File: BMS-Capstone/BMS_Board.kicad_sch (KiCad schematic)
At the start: 0 parts

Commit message: Added MP chip
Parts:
- added IC1: MP2639AGR-Z, MP2639AGRZ, symbol SamacSys_Parts:MP2639AGR-Z
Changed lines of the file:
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@@
 	(generator_version "9.0")
 	(paper "A4")
+	(symbol
+		(lib_id "SamacSys_Parts:MP2639AGR-Z")
+		(at 115.57 81.28 0)
+		(unit 1)
+		(exclude_from_sim no)
+		(in_bom yes)
+		(on_board yes)
+		(dnp no)
+		(fields_autoplaced yes)
+		(property "Reference" "IC1"
+			(at 111.76 74.8598 0)
+			(effects
+				(font
+					(size 1.27 1.27)
+				)
+			)
+		)
+		(property "Value" "MP2639AGR-Z"
+			(at 111.76 77.3998 0)
+			(effects
+				(font
+					(size 1.27 1.27)
+				)
+			)
+		)
+		(property "Footprint" "MP2639AGRZ"
+			(at 142.24 166.04 0)
+			(effects
+				(font
+					(size 1.27 1.27)
+				)
+				(justify left top)
+				(hide yes)
+			)
+		)
+		(property "Datasheet" "http://www.monolithicpower.com/pub/media/document/MP2639A_r1.0.pdf"
+			(at 142.24 266.04 0)
+			(effects
+				(font
+					(size 1.27 1.27)
+				)
+				(justify left top)
+				(hide yes)
+			)
+		)
+		(property "Description" "Battery Management 2-Cell 2.5A Li-ion or Li-polymer Switching Charger Integrated Bidirectional Charge/Discharge"
+			(at 115.57 81.28 0)
+			(effects
+				(font
+					(size 1.27 1.27)
+				)
+				(hide yes)
+			)
+		)
+		(property "Height" "1"
+			(at 142.24 466.04 0)
+			(effects
+				(font
+					(size 1.27 1.27)
+				)
+				(justify left top)
+				(hide yes)
+			)
+		)
+		(property "Manufacturer_Name" "Monolithic Power Systems (MPS)"
+			(at 142.24 566.04 0)
+			(effects
+				(font
+					(size 1.27 1.27)
+				)
+				(justify left top)
+				(hide yes)
+			)
+		)
+		(property "Manufacturer_Part_Number" "MP2639AGR-Z"
+			(at 142.24 666.04 0)
+			(effects
+				(font
+					(size 1.27 1.27)
+				)
+				(justify left top)
+				(hide yes)
+			)
+		)
+		(property "Mouser Part Number" "946-MP2639AGR-Z"
+			(at 142.24 766.04 0)
+			(effects
+				(font
+					(size 1.27 1.27)
+				)
+				(justify left top)
+				(hide yes)
+			)
+		)
+		(property "Mouser Price/Stock" "https://www.mouser.co.uk/ProductDetail/Monolithic-Power-Systems-MPS/MP2639AGR-Z?qs=YCa%2FAAYMW004W5DDRZSXeQ%3D%3D"
+			(at 142.24 866.04 0)
+			(effects
+				(font
+					(size 1.27 1.27)
+				)
+				(justify left top)
+				(hide yes)
+			)
+		)
+		(property "Arrow Part Number" ""
+			(at 142.24 966.04 0)
+			(effects
+				(font
+					(size 1.27 1.27)
+				)
+				(justify left top)
+				(hide yes)
+			)
+		)
+		(property "Arrow Price/Stock" ""
+			(at 142.24 1066.04 0)
+			(effects
+				(font
+					(size 1.27 1.27)
+				)
+				(justify left top)
+				(hide yes)
+			)
+		)
+		(pin "6"
+		)
+		(pin "25"
+		)
+		(pin "9"
+		)
+		(pin "22"
+		)
+		(pin "5"
+		)
+		(pin "7"
+		)
+		(pin "21"
+		)
+		(pin "23"
+		)
+		(pin "24"
+		)
+		(pin "8"
+		)
+		(pin "14"
+		)
+		(pin "2"
+		)
+		(pin "3"
+		)
+		(pin "1"
+		)
+		(pin "4"
+		)
+		(pin "26"
+		)
+		(pin "10"
+		)
+		(pin "12"
+		)
+		(pin "19"
+		)
+		(pin "20"
+		)
+		(pin "15"
+		)
+		(pin "11"
+		)
+		(pin "18"
+		)
+		(pin "17"
+		)
+		(pin "16"
+		)
+		(pin "13"
+		)
+		(instances
+			(project ""
+				(path "/f2da9442-ca05-4687-a880-d5cd24c39f1d/3dc06e74-ff57-4ce5-be5c-5d780b9552b6"
+					(reference "IC1")
+					(unit 1)
+				)
+			)
+		)
+	)
 )

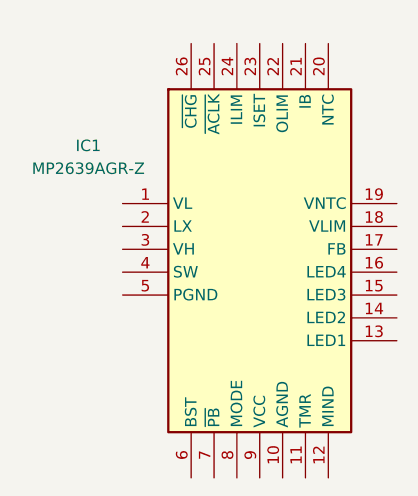
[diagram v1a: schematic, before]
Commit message: Added symbol and footprint for MP
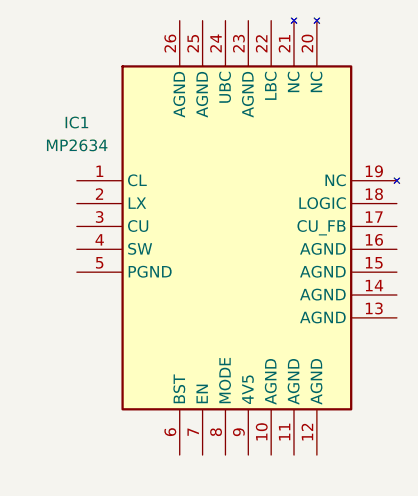
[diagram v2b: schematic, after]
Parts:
- removed IC1: MP2639AGR-Z, MP2639AGRZ, symbol SamacSys_Parts:MP2639AGR-Z
- added IC1: MP2634, SamacSys_Parts:MP2634, symbol SamacSys_Parts:MP2634
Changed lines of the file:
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@@
 	(paper "A4")
 	(symbol
-		(lib_id "SamacSys_Parts:MP2639AGR-Z")
-		(at 115.57 81.28 0)
+		(lib_id "SamacSys_Parts:MP2634")
+		(at 115.57 78.74 0)
 		(unit 1)
 		(exclude_from_sim no)
@@
 		(fields_autoplaced yes)
 		(property "Reference" "IC1"
-			(at 111.76 74.8598 0)
+			(at 110.49 72.3198 0)
 			(effects
 				(font
@@
 			)
 		)
-		(property "Value" "MP2639AGR-Z"
-			(at 111.76 77.3998 0)
+		(property "Value" "MP2634"
+			(at 110.49 74.8598 0)
 			(effects
 				(font
@@
 			)
 		)
-		(property "Footprint" "MP2639AGRZ"
-			(at 142.24 166.04 0)
+		(property "Footprint" "SamacSys_Parts:MP2634"
+			(at 142.24 163.5 0)
 			(effects
 				(font
@@
 		)
 		(property "Datasheet" "http://www.monolithicpower.com/pub/media/document/MP2639A_r1.0.pdf"
-			(at 142.24 266.04 0)
+			(at 142.24 263.5 0)
 			(effects
 				(font
@@
 			)
 		)
-		(property "Description" "Battery Management 2-Cell 2.5A Li-ion or Li-polymer Switching Charger Integrated Bidirectional Charge/Discharge"
-			(at 115.57 81.28 0)
+		(property "Description" "Integrated, 2A, BidirectionalActive Balancer"
+			(at 128.016 49.53 0)
 			(effects
 				(font
@@
 		)
 		(property "Height" "1"
-			(at 142.24 466.04 0)
+			(at 142.24 463.5 0)
 			(effects
 				(font
@@
 		)
 		(property "Manufacturer_Name" "Monolithic Power Systems (MPS)"
-			(at 142.24 566.04 0)
+			(at 142.24 563.5 0)
 			(effects
 				(font
@@
 		)
 		(property "Manufacturer_Part_Number" "MP2639AGR-Z"
-			(at 142.24 666.04 0)
+			(at 142.24 663.5 0)
 			(effects
 				(font
@@
 		)
 		(property "Mouser Part Number" "946-MP2639AGR-Z"
-			(at 142.24 766.04 0)
+			(at 142.24 763.5 0)
 			(effects
 				(font
@@
 		)
 		(property "Mouser Price/Stock" "https://www.mouser.co.uk/ProductDetail/Monolithic-Power-Systems-MPS/MP2639AGR-Z?qs=YCa%2FAAYMW004W5DDRZSXeQ%3D%3D"
-			(at 142.24 866.04 0)
+			(at 142.24 863.5 0)
 			(effects
 				(font
@@
 		)
 		(property "Arrow Part Number" ""
-			(at 142.24 966.04 0)
+			(at 142.24 963.5 0)
 			(effects
 				(font
@@
 		)
 		(property "Arrow Price/Stock" ""
-			(at 142.24 1066.04 0)
+			(at 142.24 1063.5 0)
 			(effects
 				(font
@@
 		(pin "6"
 		)
-		(pin "25"
+		(pin "18"
 		)
-		(pin "9"
+		(pin "20"
+		)
+		(pin "15"
+		)
+		(pin "1"
 		)
 		(pin "22"
 		)
-		(pin "5"
+		(pin "25"
 		)
-		(pin "7"
-		)
-		(pin "21"
-		)
-		(pin "23"
-		)
-		(pin "24"
-		)
-		(pin "8"
-		)
-		(pin "14"
-		)
-		(pin "2"
-		)
-		(pin "3"
-		)
-		(pin "1"
-		)
-		(pin "4"
+		(pin "11"
 		)
 		(pin "26"
@@
 		(pin "10"
 		)
-		(pin "12"
+		(pin "21"
+		)
+		(pin "7"
+		)
+		(pin "5"
+		)
+		(pin "24"
 		)
 		(pin "19"
 		)
-		(pin "20"
+		(pin "23"
 		)
-		(pin "15"
+		(pin "9"
 		)
-		(pin "11"
+		(pin "2"
 		)
-		(pin "18"
+		(pin "8"
+		)
+		(pin "3"
+		)
+		(pin "4"
+		)
+		(pin "12"
 		)
 		(pin "17"
@@
 		(pin "13"
 		)
+		(pin "14"
+		)
 		(instances

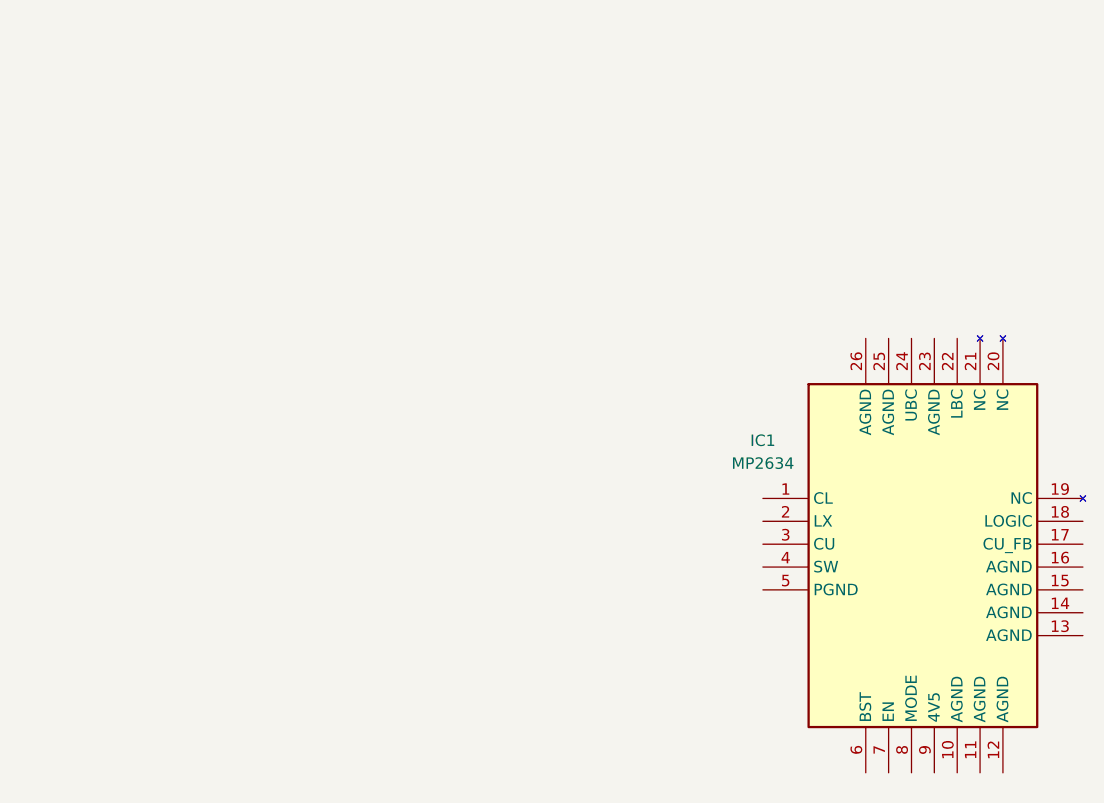
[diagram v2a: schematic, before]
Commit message: Created Schematic for MP chip
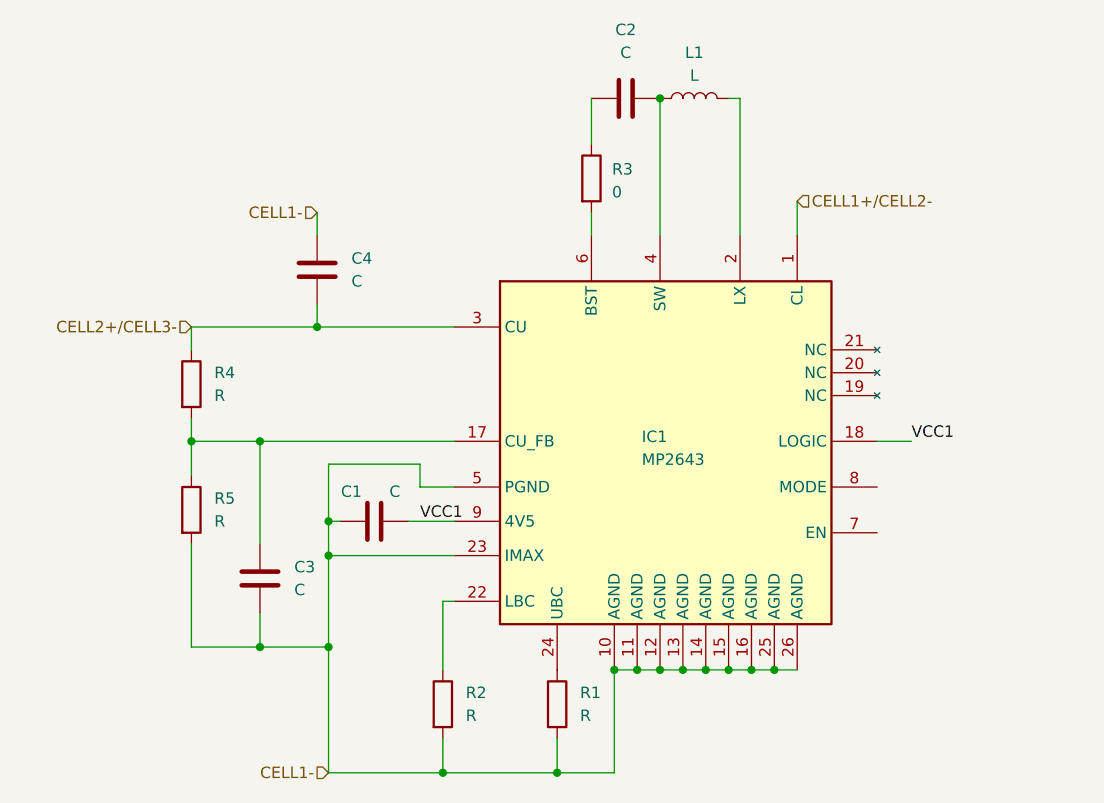
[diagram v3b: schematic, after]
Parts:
- removed IC1: MP2634, SamacSys_Parts:MP2634, symbol SamacSys_Parts:MP2634
- added C1, C2, C3, C4: C, Capacitor_SMD:C_0805_2012Metric, symbol Device:C
- added IC1: MP2643, SamacSys_Parts:MP2639AGRZ, symbol SamacSys_Parts:MP2643
- added L1: L, symbol Device:L
- added R1, R2, R4, R5: R, Resistor_SMD:R_0805_2012Metric, symbol Device:R
- added R3: 0, Resistor_SMD:R_0805_2012Metric, symbol Device:R
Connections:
- new net: C3.2, IC1.17 (CU_FB), R4.2, R5.1
- new net: C2.2, IC1.4 (SW), L1.1
- new net: IC1.2 (LX), L1.2
- new net: IC1.22 (LBC), R2.1
- new net: IC1.24 (UBC), R1.1
- new net: IC1.6 (BST), R3.2
- new net: C2.1, R3.1
- new net CELL1+/CELL2-: IC1.1 (CL)
- new net CELL1-: C1.1, C3.1, C4.2, IC1.10 (AGND), IC1.11 (AGND), IC1.12 (AGND), IC1.13 (AGND), IC1.14 (AGND), IC1.15 (AGND), IC1.16 (AGND), IC1.23 (IMAX), IC1.25 (AGND), IC1.26 (AGND), IC1.5 (PGND), R1.2, R2.2, R5.2
- new net CELL2+/CELL3-: C4.1, IC1.3 (CU), R4.1
- new net VCC1: C1.2, IC1.18 (LOGIC), IC1.9 (4V5)

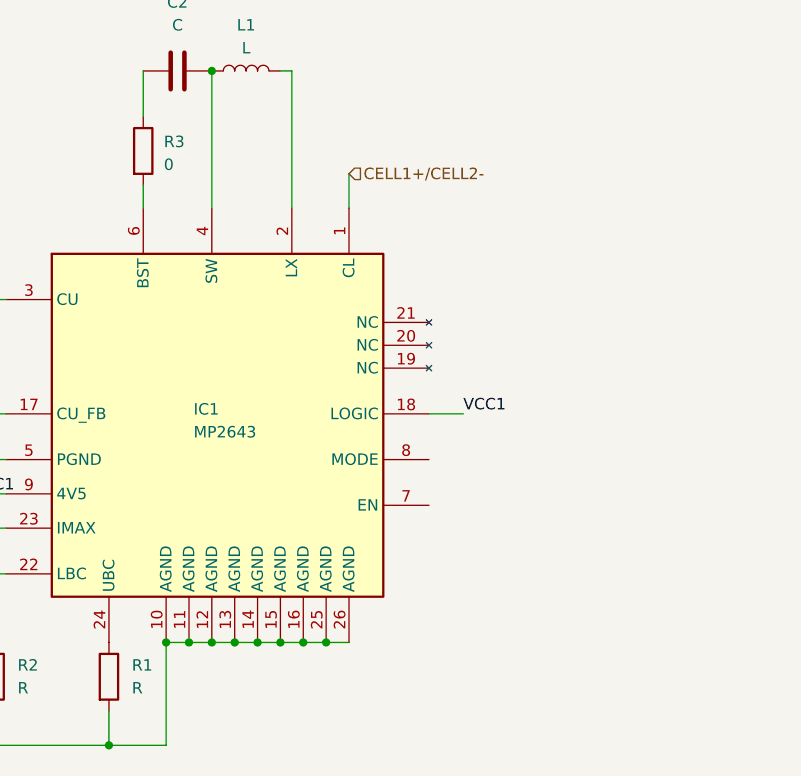
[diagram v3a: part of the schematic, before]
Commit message: Designed one entire MP chip layout
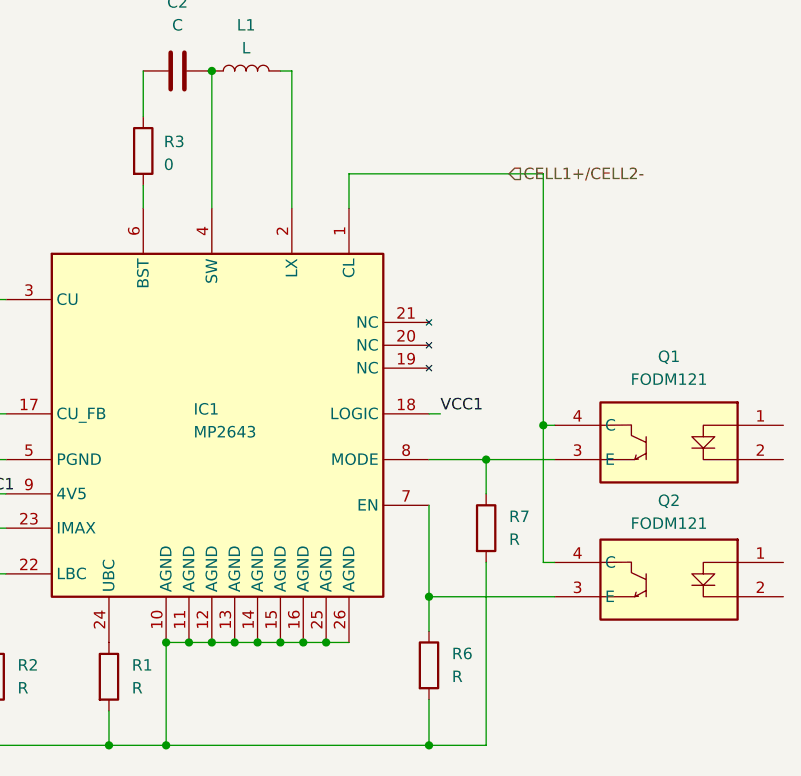
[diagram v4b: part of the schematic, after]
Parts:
- added Q1, Q2: FODM121, SOP254P675X240-4N, symbol SamacSys_Parts:FODM121
- added R6, R7: R, Resistor_SMD:R_0805_2012Metric, symbol Device:R
- L1: footprint (none) -> SamacSys_Parts:MPLAL4020R47 Inductor
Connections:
- net CELL1+/CELL2-: now also Q1.4 (C), Q2.4 (C)
- net CELL1-: now also R6.2, R7.2
- net at IC1.7 (EN): now also Q2.3 (E), R6.1
- net at IC1.8 (MODE): now also Q1.3 (E), R7.1

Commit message: More fixes
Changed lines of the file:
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@@
-	(wire
-		(pts
-			(xy 135.89 45.72) (xy 114.3 45.72)
-		)
-		(stroke
-			(width 0)
-			(type default)
-		)
-	)
 	(wire
 		(pts
@@
 		(pts
 			(xy 46.99 72.39) (xy 54.61 72.39)
+		)
+		(stroke
+			(width 0)
+			(type default)
+		)
+	)
+	(wire
+		(pts
+			(xy 114.3 45.72) (xy 135.89 45.72)
 		)
 		(stroke
@@
 	(hierarchical_label "CELL1+{slash}CELL2-"
 		(shape input)
-		(at 132.08 45.72 0)
-		(effects
-			(font
+		(at 135.89 45.72 0)
+		(effects
+			(font

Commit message: added CL capacitor
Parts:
- added C5: C, Capacitor_SMD:C_0805_2012Metric, symbol Device:C
- Q1, Q2: footprint SOP254P675X240-4N -> SamacSys_Parts:SOP254P675X240-4N
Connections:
- net CELL1+/CELL2-: now also C5.1
- net CELL1-: now also C5.2
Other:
- moved on the sheet: C1, C2, C3, C4, IC1, L1, Q1, Q2, R1, R2, R3, R4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

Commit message: Slight modifications
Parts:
- added C10, C6, C7, C8, C9: C, Capacitor_SMD:C_0805_2012Metric, symbol Device:C
- added IC2: MP2643, SamacSys_Parts:MP2639AGRZ, symbol SamacSys_Parts:MP2643
- added L2: L, SamacSys_Parts:MPLAL4020R47 Inductor, symbol Device:L
- added Q3, Q4: FODM121, SamacSys_Parts:SOP254P675X240-4N, symbol SamacSys_Parts:FODM121
- added R10: 0, Resistor_SMD:R_0805_2012Metric, symbol Device:R
- added R11, R12, R13, R14, R8, R9: R, Resistor_SMD:R_0805_2012Metric, symbol Device:R
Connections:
- net CELL1+/CELL2-: now also C10.2, C6.1, C7.2, C8.1, IC2.10 (AGND), IC2.11 (AGND), IC2.12 (AGND), IC2.13 (AGND), IC2.14 (AGND), IC2.15 (AGND), IC2.16 (AGND), IC2.23 (IMAX), IC2.25 (AGND), IC2.26 (AGND), IC2.5 (PGND), R10.2, R11.2, R13.2, R14.2, R9.2
- net CELL2+/CELL3-: now also C10.1, IC2.1 (CL), Q3.4 (C), Q4.4 (C)
- new net: IC2.7 (EN), Q4.3 (E), R13.1
- new net: IC2.8 (MODE), Q3.3 (E), R14.1
- new net: C9.1, R12.1
- new net: C9.2, IC2.4 (SW), L2.1
- new net: C6.2, IC2.17 (CU_FB), R8.2, R9.1
- new net: IC2.22 (LBC), R10.1
- new net: IC2.2 (LX), L2.2
- new net: IC2.24 (UBC), R11.1
- new net: IC2.6 (BST), R12.2
- new net CELL3+/CELL4-: C7.1, IC2.3 (CU), R8.1
- new net VCC2: C8.2, IC2.18 (LOGIC), IC2.9 (4V5)
